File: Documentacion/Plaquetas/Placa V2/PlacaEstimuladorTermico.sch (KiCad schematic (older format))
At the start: 64 parts, among them J1 Conn_01x02, J2 DB9_Female_MountingHoles, J4 BORNERA_VCC, K1 Modulo_Relé, Q1 IRF4905, Q2 IRFZ44N, Q3 IRF4905, Q4 IRFZ44N, Q5 BC337, Q6 BC337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

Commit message: Add files via upload
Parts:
- removed J4: BORNERA_VCC, TerminalBlock:TerminalBlock_bornier-2_P5.08mm, symbol Connector:Screw_Terminal_01x02
- added J3, J4: Conn_01x01, Connector:Banana_Jack_1Pin, symbol Connector_Generic:Conn_01x01
- added J5: Conn_01x02, custom_footprints:disipadorFETS, symbol Connector_Generic:Conn_01x02
- C10, C11: footprint Capacitor_THT:C_Disc_D9.0mm_W5.0mm_P10.00mm -> Capacitor_SMD:C_1206_3216Metric_Pad1.42x1.75mm_HandSolder
- C3, C4, C5, C6, C9: footprint Capacitor_THT:C_Disc_D7.0mm_W2.5mm_P5.00mm -> Capacitor_SMD:C_1206_3216Metric_Pad1.42x1.75mm_HandSolder
- C8: footprint Capacitor_THT:C_Disc_D12.0mm_W4.4mm_P7.75mm -> Capacitor_SMD:C_1206_3216Metric_Pad1.42x1.75mm_HandSolder
- R1, R13, R2: footprint Resistor_THT:R_Axial_DIN0204_L3.6mm_D1.6mm_P5.08mm_Horizontal -> Resistor_SMD:R_1206_3216Metric
- R11, R12: footprint Resistor_THT:R_Axial_DIN0309_L9.0mm_D3.2mm_P15.24mm_Horizontal -> Resistor_SMD:R_1206_3216Metric
- R14, R15: footprint Resistor_SMD:R_0805_2012Metric -> Resistor_SMD:R_1206_3216Metric
- RV1: footprint Potentiometer_THT:Potentiometer_ACP_CA14-H2,5_Horizontal -> Potentiometer_THT:Potentiometer_Bourns_3266Y_Vertical
- U1: footprint Package_DIP:DIP-14_W7.62mm_LongPads -> Package_DIP:DIP-14_W8.89mm_SMDSocket_LongPads
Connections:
- net GND: now also J2.5, K1.2 (DC-), J4.1 (Pin_1); no longer J2.6, K1.3 (IN)
- net PIN-READY-LED-GREEN: now also A1.7 (D4); no longer A1.15 (D12)
- net PIN_SENSOR_TEMPERATURA_PUNTUAL: now also A1.20 (A1); no longer A1.21 (A2)
- net PIN_SENSOR_TEMPERATURA_SUPERFICIAL: now also A1.21 (A2); no longer A1.20 (A1)
- net PMOS_CALOR: now also A1.9 (D6); no longer A1.10 (D7)
- net PMOS_FRIO: now also A1.8 (D5); no longer A1.11 (D8)
- net PWM_CALOR: now also A1.10 (D7); no longer A1.8 (D5)
- net PWM_FRIO: now also A1.11 (D8); no longer A1.9 (D6)
- net VCC: now also J2.9, K1.3 (IN), J3.1 (Pin_1); no longer J2.5, K1.2 (DC-)
- no-connect marks 22 -> 24
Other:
- note added: "Disipador mosfets"

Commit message: Correction of all the errors in the pcb
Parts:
- removed D6: D_Zener, Diode_THT:D_DO-201AE_P12.70mm_Horizontal, symbol Device:D_Zener
- removed R16: R, Resistor_SMD:R_1206_3216Metric, symbol Device:R
- added J6: Pulsador OFF, TerminalBlock:TerminalBlock_bornier-2_P5.08mm, symbol Connector:Screw_Terminal_01x02
- added J7, J8: Conn_02x04_Counter_Clockwise, Package_DIP:DIP-8_W7.62mm_LongPads, symbol Connector_Generic:Conn_02x04_Counter_Clockwise
- added R21, R22: 15, Resistor_THT:R_Axial_DIN0204_L3.6mm_D1.6mm_P5.08mm_Horizontal, symbol Device:R
- added U6: TL431LP, Package_TO_SOT_THT:TO-92_Inline, symbol Reference_Voltage:TL431LP
- SW1: value SW_DIP_x01 -> Pulsador ON
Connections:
- net labels added: fan_1C, fan_2C, term_disip_1C, term_disip_2C, term_pelt_1C, term_pelt_2C
- wire segments 220 -> 293
- no-connect marks 24 -> 23
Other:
- note added: "Pines macho de 2x4 para \nconector de cable plano\n"
- note added: "Placa de conexion DB9 a conector de cable plano\n"
- moved on the sheet: D5, J2, R17, RV1, SW1, U1B

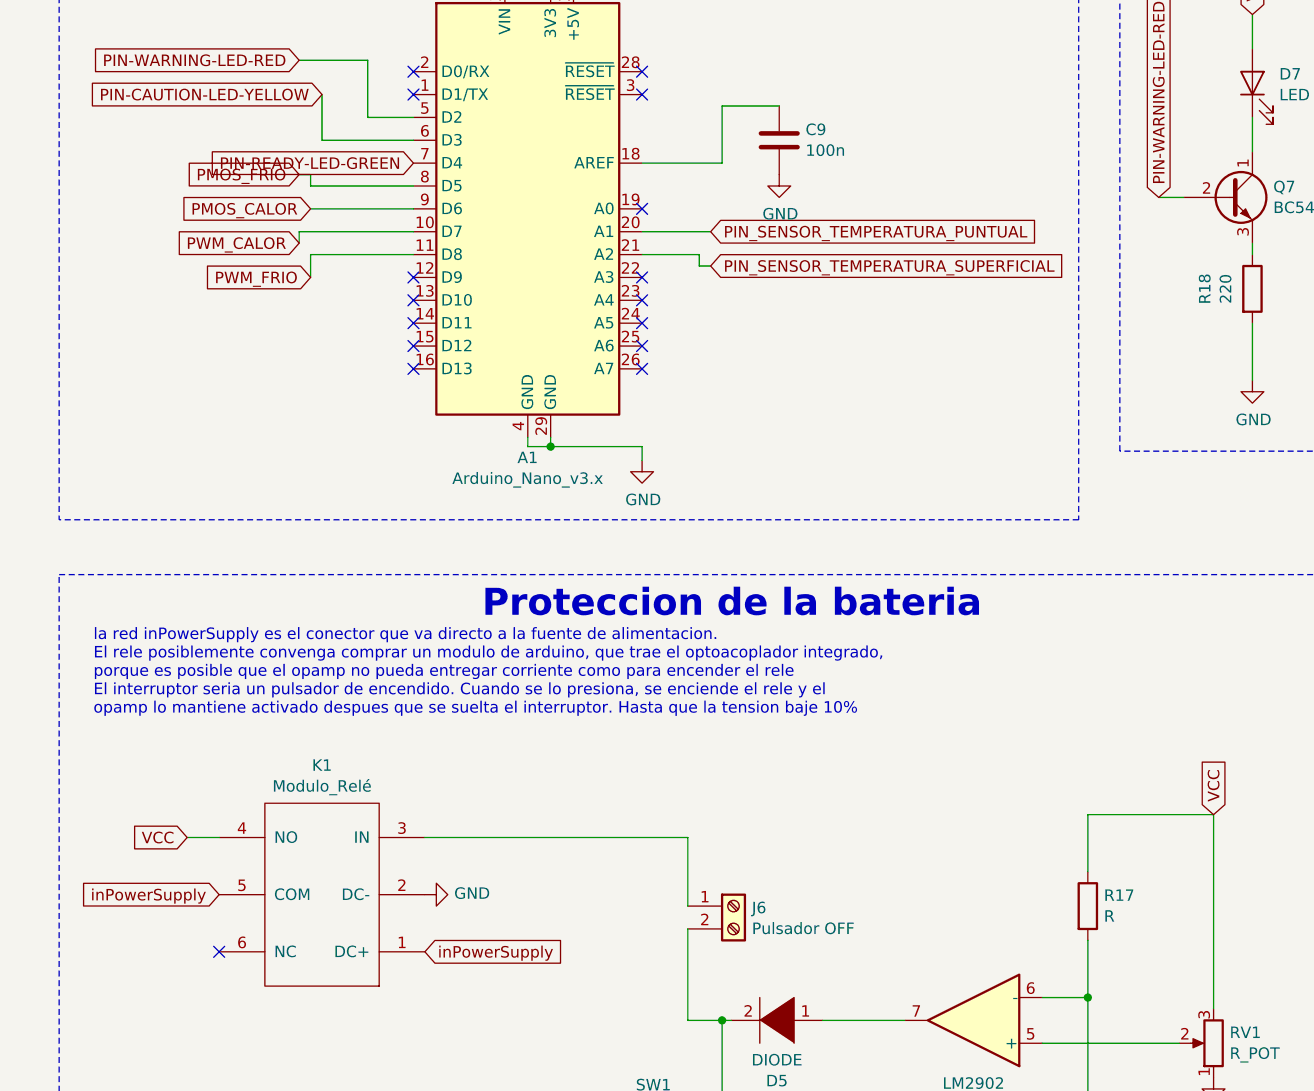
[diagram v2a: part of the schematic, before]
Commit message: Correction of pwm pins
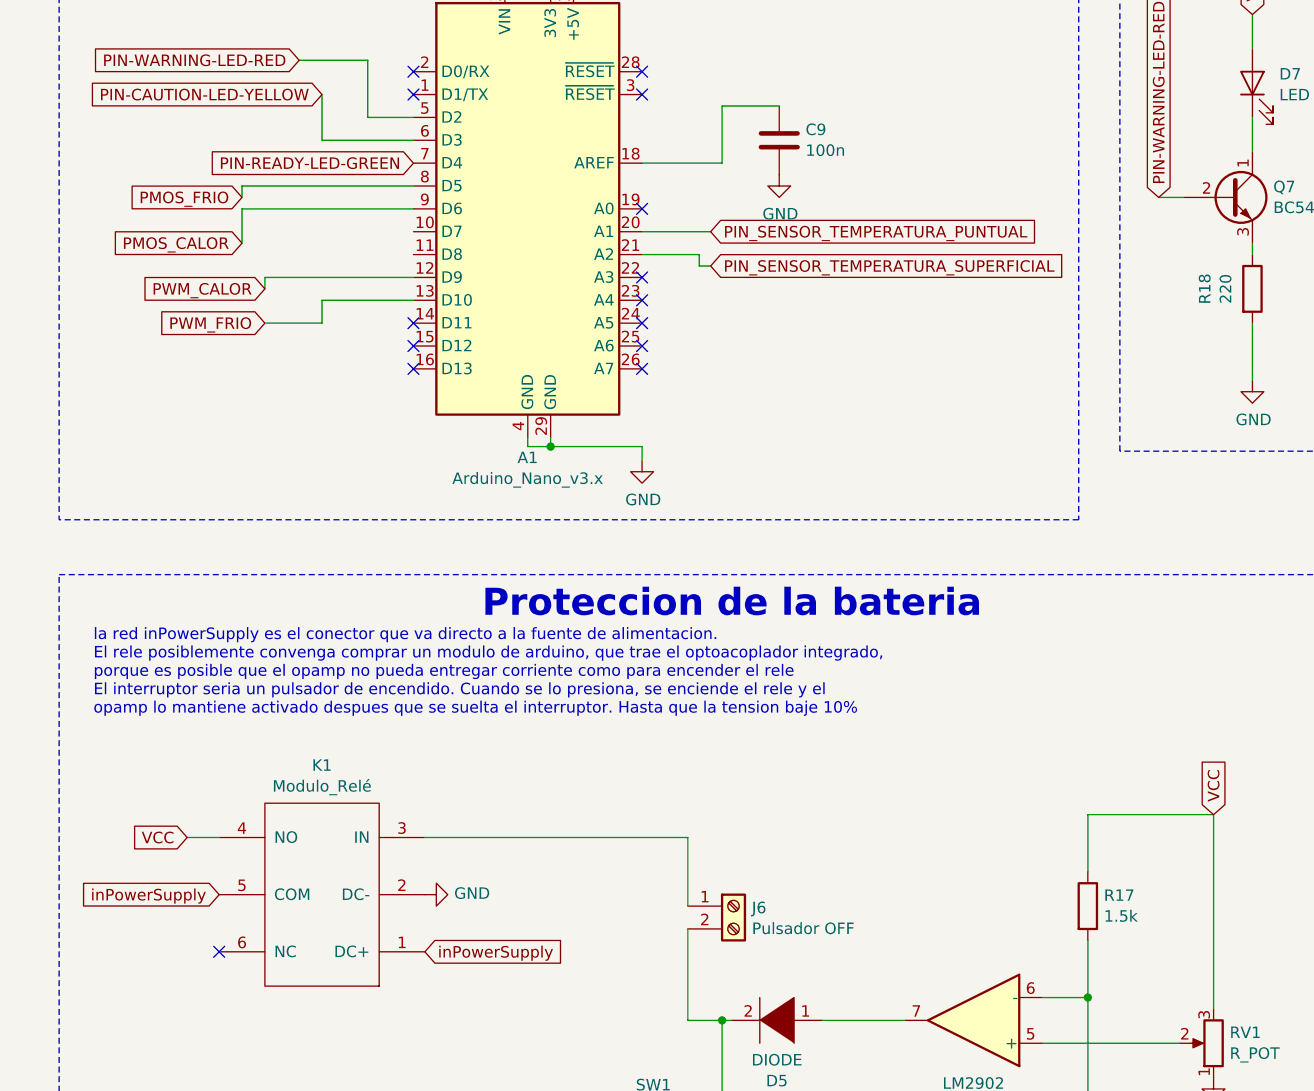
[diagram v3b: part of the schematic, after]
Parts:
- R17: value R -> 1.5k
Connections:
- wire segments 293 -> 294
- no-connect marks 23 -> 21
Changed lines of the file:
@@
 Text GLabel 4670 2970 0    50   Input ~ 0
 PWM_CALOR
-Text GLabel 1750 5900 0    50   Input ~ 0
+Text GLabel 1550 6100 0    50   Input ~ 0
 PWM_FRIO
-Text GLabel 1700 5750 0    50   Input ~ 0
+Text GLabel 1550 5950 0    50   Input ~ 0
 PWM_CALOR
-Wire Wire Line
-	1750 5600 2200 5600
-Wire Wire Line
-	1700 5450 1750 5450
-Wire Wire Line
-	1750 5450 1750 5500
-Wire Wire Line
-	1750 5500 2200 5500
-Text GLabel 1750 5600 0    50   Input ~ 0
+Text GLabel 1450 5750 0    50   Input ~ 0
 PMOS_CALOR
-Text GLabel 1700 5450 0    50   Input ~ 0
+Text GLabel 1450 5550 0    50   Input ~ 0
 PMOS_FRIO
-Wire Wire Line
-	2200 5700 1700 5700
-Wire Wire Line
-	1700 5700 1700 5750
-Wire Wire Line
-	2200 5800 1750 5800
-Wire Wire Line
-	1750 5800 1750 5900
 $Comp
 L power:GND #PWR04
@@
 P 5150 8650
 F 0 "R17" H 5220 8696 50  0000 L CNN
-F 1 "R" H 5220 8605 50  0000 L CNN
+F 1 "1.5k" H 5220 8605 50  0000 L CNN
 F 2 "Resistor_SMD:R_1206_3216Metric" V 5080 8650 50  0001 C CNN
 F 3 "~" H 5150 8650 50  0001 C CNN
@@
 NoConn ~ 2200 5000
 NoConn ~ 2200 5100
-NoConn ~ 2200 5900
-NoConn ~ 2200 6000
 NoConn ~ 2200 6100
 NoConn ~ 2600 4600
@@
 Wire Wire Line
 	5150 10100 5150 10650
+Wire Wire Line
+	2200 5500 1450 5500
+Wire Wire Line
+	1450 5500 1450 5550
+Wire Wire Line
+	1450 5750 1450 5600
+Wire Wire Line
+	1450 5600 2200 5600
+Wire Wire Line
+	2200 5900 1550 5900
+Wire Wire Line
+	1550 5900 1550 5950
+Wire Wire Line
+	1550 6100 1800 6100
+Wire Wire Line
+	1800 6100 1800 6000
+Wire Wire Line
+	1800 6000 2200 6000
 $EndSCHEMATC

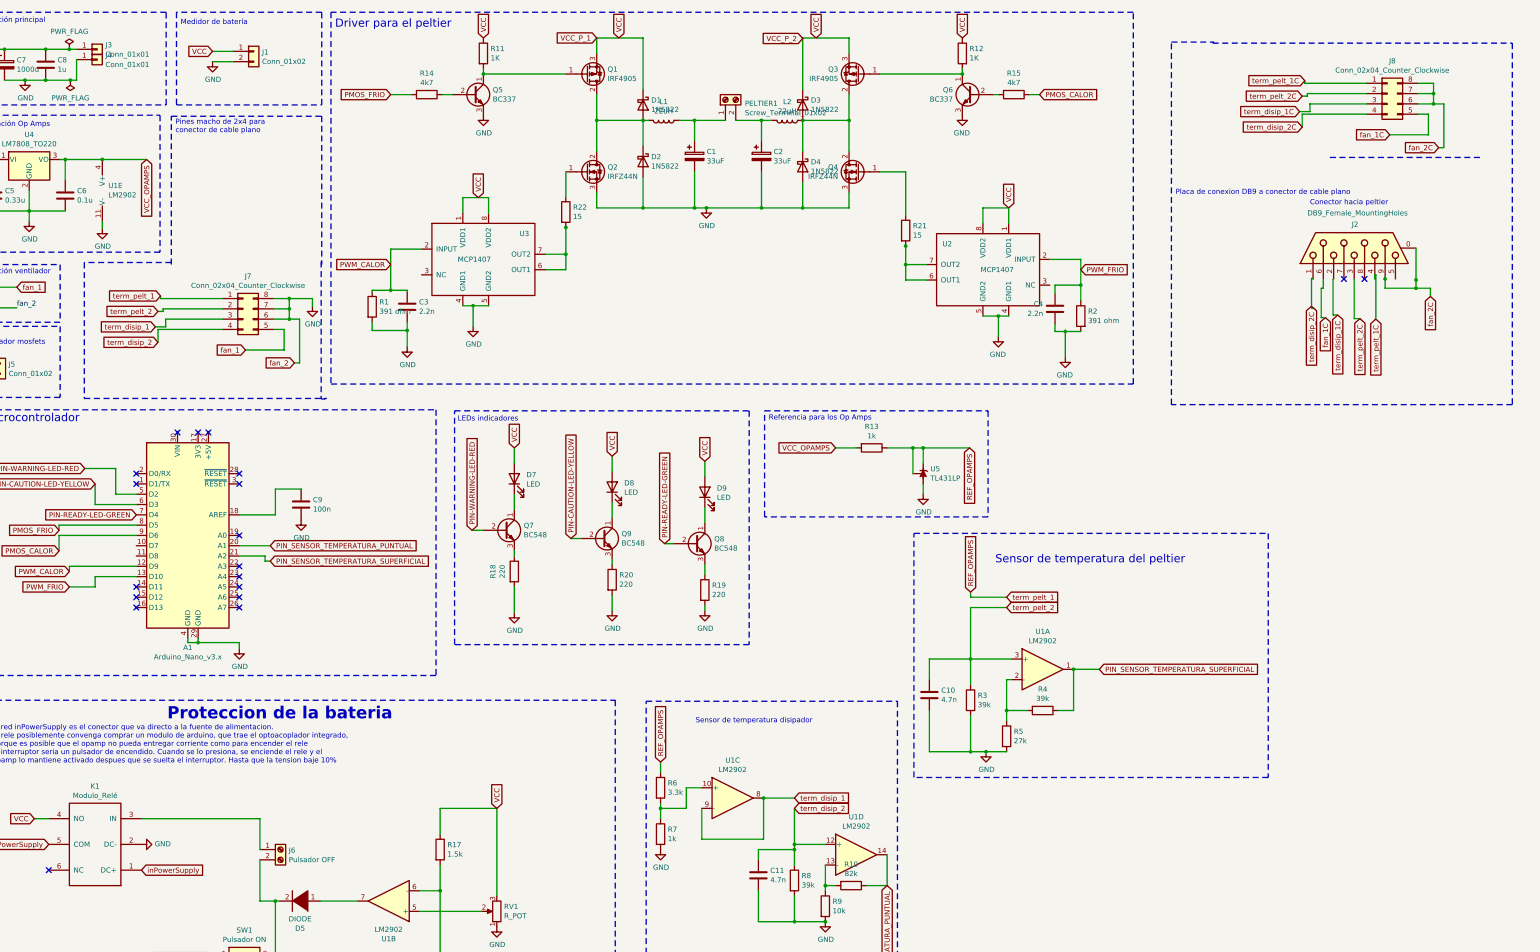
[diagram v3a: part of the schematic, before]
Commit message: Modification of the main board, add of leds circuit and db9 board
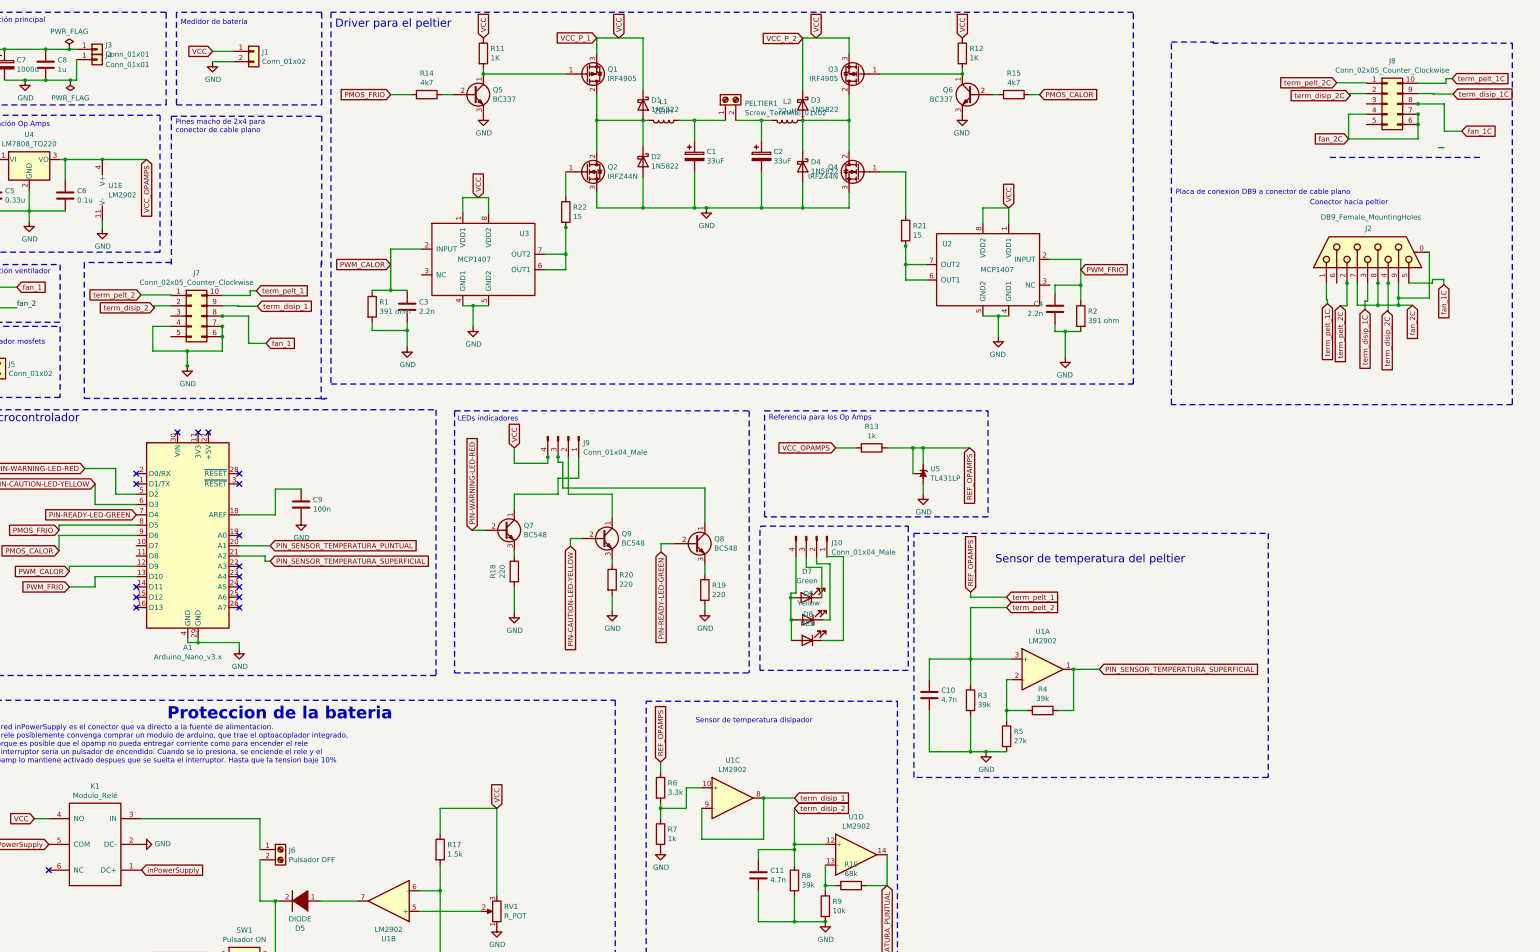
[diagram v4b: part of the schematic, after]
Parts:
- removed D9: LED, TerminalBlock:TerminalBlock_bornier-2_P5.08mm, symbol Device:LED
- removed J7, J8: Conn_02x04_Counter_Clockwise, Package_DIP:DIP-8_W7.62mm_LongPads, symbol Connector_Generic:Conn_02x04_Counter_Clockwise
- added D6: Yellow, symbol Device:LED
- added J10, J9: Conn_01x04_Male, Connector_PinHeader_2.54mm:PinHeader_1x04_P2.54mm_Vertical, symbol Connector:Conn_01x04_Male
- added J7: Conn_02x05_Counter_Clockwise, Connector_PinHeader_2.54mm:PinHeader_2x05_P2.54mm_VerticalNico, symbol Connector_Generic:Conn_02x05_Counter_Clockwise
- added J8: Conn_02x05_Counter_Clockwise, Connector_PinHeader_2.54mm:PinHeader_2x05_P2.54mm_Vertical, symbol Connector_Generic:Conn_02x05_Counter_Clockwise
- D7: value LED -> Green; footprint TerminalBlock:TerminalBlock_bornier-2_P5.08mm -> (none)
- D8: value LED -> RED; footprint TerminalBlock:TerminalBlock_bornier-2_P5.08mm -> (none)
- R10: value 82k -> 68k
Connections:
- wire segments 294 -> 326
- no-connect marks 21 -> 19
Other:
- moved on the sheet: J2

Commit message: Modifications in the schematic
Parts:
- D6, D7, D8: footprint (none) -> Diode_THT:D_A-405_P7.62mm_Horizontal
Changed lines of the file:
@@
 F 0 "D6" H 8713 6165 50  0000 C CNN
 F 1 "Yellow" H 8713 6256 50  0000 C CNN
-F 2 "" H 8720 6420 50  0001 C CNN
+F 2 "Diode_THT:D_A-405_P7.62mm_Horizontal" H 8720 6420 50  0001 C CNN
 F 3 "~" H 8720 6420 50  0001 C CNN
 	1    8720 6420
@@
 F 0 "D7" H 8698 5950 50  0000 C CNN
 F 1 "Green" H 8698 6041 50  0000 C CNN
-F 2 "" H 8705 6205 50  0001 C CNN
+F 2 "Diode_THT:D_A-405_P7.62mm_Horizontal" H 8705 6205 50  0001 C CNN
 F 3 "~" H 8705 6205 50  0001 C CNN
 	1    8705 6205
@@
 F 0 "D8" H 8708 6365 50  0000 C CNN
 F 1 "RED" H 8708 6456 50  0000 C CNN
-F 2 "" H 8715 6620 50  0001 C CNN
+F 2 "Diode_THT:D_A-405_P7.62mm_Horizontal" H 8715 6620 50  0001 C CNN
 F 3 "~" H 8715 6620 50  0001 C CNN
 	1    8715 6620
